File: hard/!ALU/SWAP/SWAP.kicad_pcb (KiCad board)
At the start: 2 copper layers, 61 x 26.7 mm, 7 parts, among them J2 Conn_01x08_Male, J3 Conn_01x08_Male, J4 Conn_01x04_Male, U1 74LS573

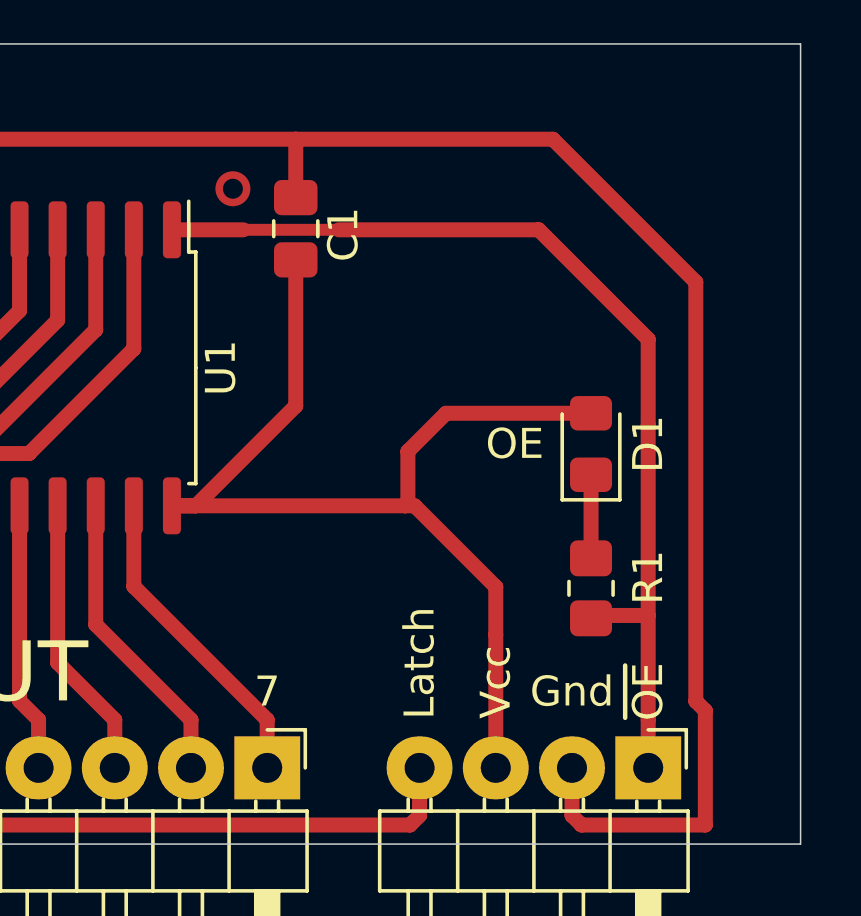
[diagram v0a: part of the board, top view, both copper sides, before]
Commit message: KiCAD 5 -> 9
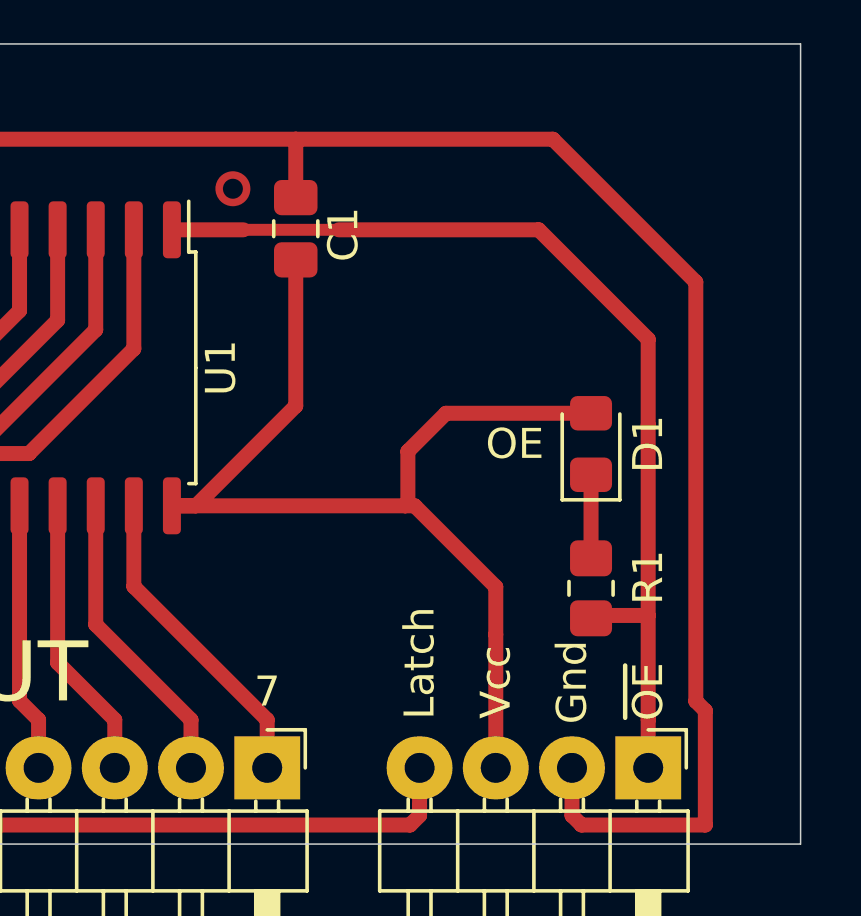
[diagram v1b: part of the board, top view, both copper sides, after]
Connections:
- net /~OE renamed /~{OE}
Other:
- net class Default removed
- board text added: "~{OE}"
- board text removed: "~OE"
